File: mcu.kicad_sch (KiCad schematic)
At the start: 141 parts, among them Q10 BSS138W, Q3 BSS138W, Q4 BSS138W, Q5 BSS138W, Q6 BSS138W, Q7 BSS138W, Q8 BSS138W, Q9 BSS138W, SW1 TS110926043, SW2 TS110926043, U1 PIC32CK1025GC01100-I/4SB, X2 Q13FC13500004, X3 X322512MSB4SI

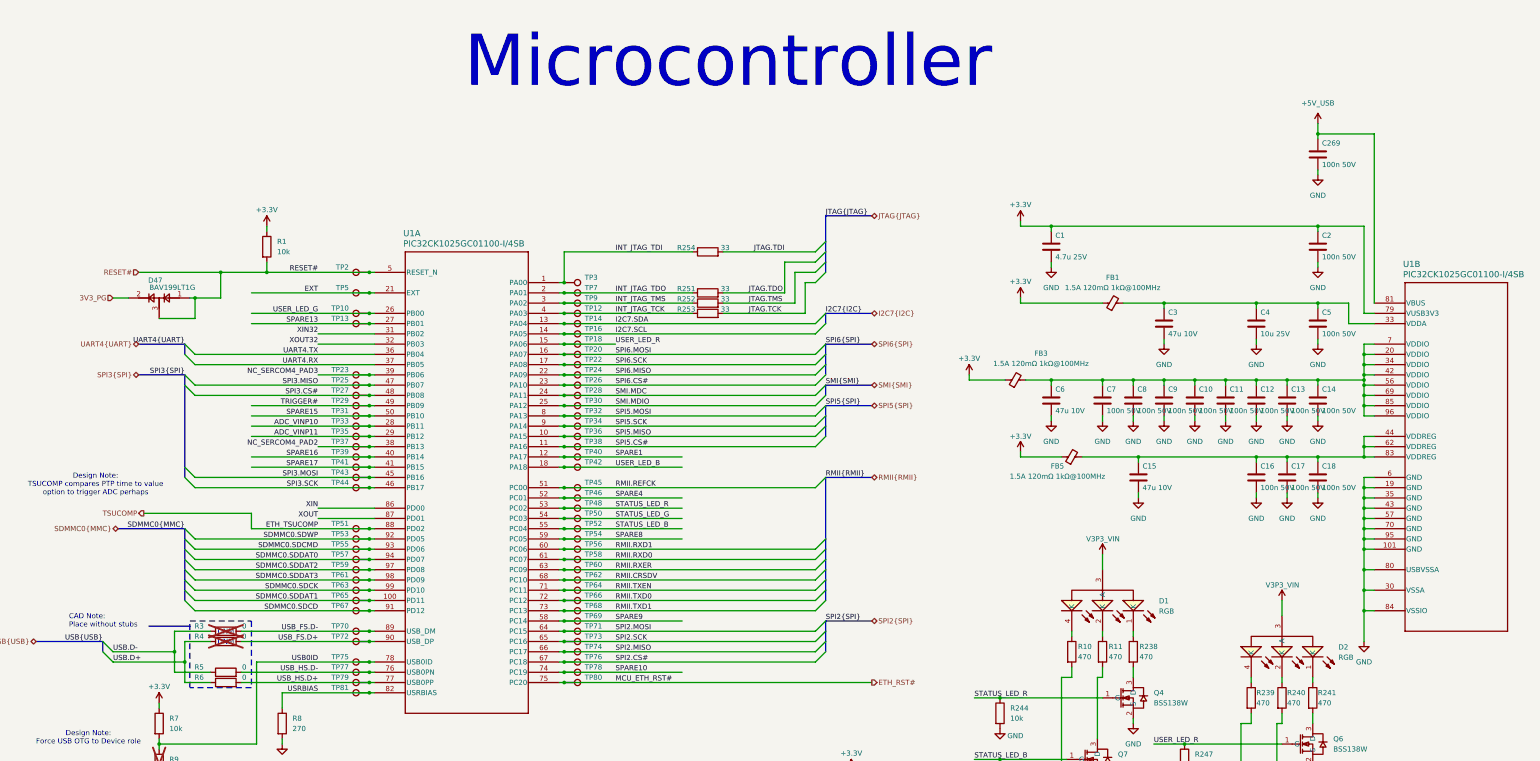
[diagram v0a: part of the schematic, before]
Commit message: fixed some more schematic review
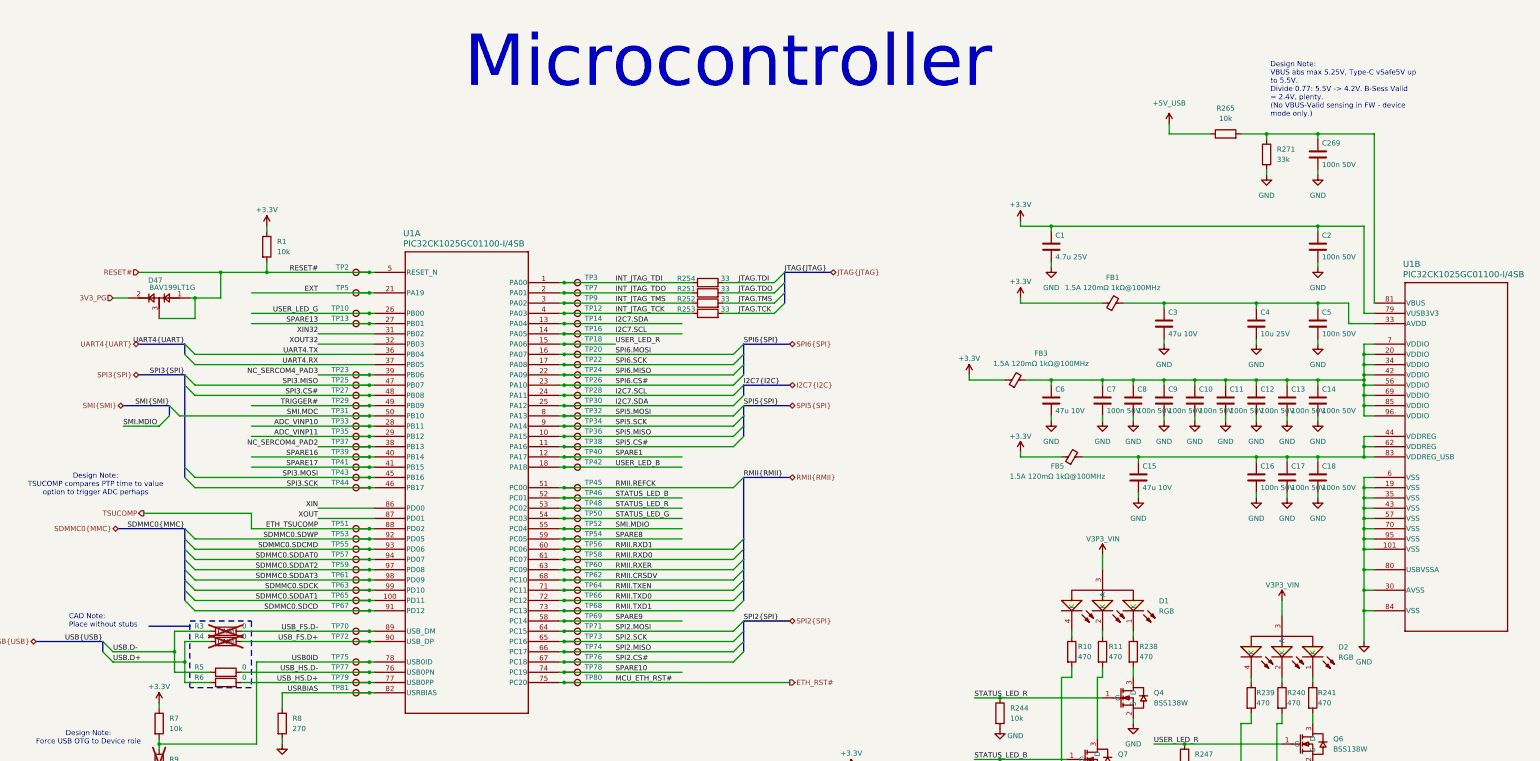
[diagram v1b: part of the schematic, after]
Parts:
- added R265: 10k, Resistor_SMD:R_0402_1005Metric, symbol Device:R
- added R271: 33k, Resistor_SMD:R_0603_1608Metric, symbol Device:R
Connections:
- net SPARE15 is gone; now on net SMI.MDC: TP31.1, U1.50 (PB10)
- net SPARE4 is gone; now on net STATUS_LED_B: TP46.1, U1.52 (PC01)
- net +5V_USB: now also R265.1; no longer C269.1, U1.81 (VBUS)
- net GND: now also R271.2
- net I2C7.SCL: now also TP28.1, U1.24 (PA11)
- net I2C7.SDA: now also TP30.1, U1.25 (PA12)
- net SMI.MDC: no longer TP28.1, U1.24 (PA11)
- net SMI.MDIO: now also TP52.1, U1.55 (PC04); no longer TP30.1, U1.25 (PA12)
- net STATUS_LED_B: no longer TP52.1, U1.55 (PC04)
- new net: C269.1, R265.2, R271.1, U1.81 (VBUS)
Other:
- moved on the sheet: R254

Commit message: did a bit of placement
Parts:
- removed TP45, TP54, TP56, TP58, TP62: TestPoint, TestPoint:TestPoint_THTPad_D1.0mm_Drill0.5mm, symbol Connector:TestPoint

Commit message: did some layout
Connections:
- net MCU_VDDREG: now reaches C15.1, C16.1, C17.1, C18.1, FB5.2, U1.44 (VDDREG), U1.62 (VDDREG), U1.83 (VDDREG_USB)
- net MCU_VDDIO: now reaches C10.1, C11.1, C12.1, C13.1, C14.1, C6.1, C7.1, C8.1, C9.1, FB3.2, U1.20 (VDDIO), U1.34 (VDDIO), U1.42 (VDDIO), U1.56 (VDDIO), U1.69 (VDDIO), U1.7 (VDDIO), U1.85 (VDDIO), U1.96 (VDDIO)
- net MCU_AVDD: now reaches C3.1, C4.1, C5.1, FB1.2, U1.33 (AVDD)
- net MCU_VBUS: now reaches C269.1, R265.2, R271.1, U1.81 (VBUS)
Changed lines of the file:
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@@
 		)
 	)
+	(label "MCU_VDDIO"
+		(at 318.77 116.84 0)
+		(effects
+			(font
+				(size 1.27 1.27)
+			)
+			(justify left bottom)
+		)
+	)
 	(label "SDMMC0.SDDAT0"
 		(at 100.33 161.29 180)
@@
 		)
 	)
+	(label "MCU_AVDD"
+		(at 320.04 97.79 0)
+		(effects
+			(font
+				(size 1.27 1.27)
+			)
+			(justify left bottom)
+		)
+	)
 	(label "RMII.RXER"
 		(at 173.99 163.83 0)
@@
 		)
 	)
+	(label "MCU_VBUS"
+		(at 341.63 55.88 0)
+		(effects
+			(font
+				(size 1.27 1.27)
+			)
+			(justify left bottom)
+		)
+	)
 	(label "TRIGGER#"
 		(at 229.87 224.79 180)
@@
 		)
 	)
+	(label "MCU_VDDREG"
+		(at 317.5 135.89 0)
+		(effects
+			(font
+				(size 1.27 1.27)
+			)
+			(justify left bottom)
+		)
+	)
 	(label "JTAG.TDO"
 		(at 204.47 95.25 0)
@@
 		)
 	)
+	(embedded_fonts no)
 )

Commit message: did a lot of layout
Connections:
- net I2C7.SCL: no longer TP16.1, U1.14 (PA05)
- net I2C7.SDA: no longer TP14.1, U1.13 (PA04)
- new net NC_PA4: TP14.1, U1.13 (PA04)
- new net NC_PA5: TP16.1, U1.14 (PA05)
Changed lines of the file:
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@@
 		)
 	)
-	(label "I2C7.SDA"
+	(label "NC_PA4"
 		(at 173.99 102.87 0)
 		(effects
 			(font
 				(size 1.27 1.27)
+				(color 0 18 255 1)
 			)
 			(justify left bottom)
@@
 		)
 	)
-	(label "I2C7.SCL"
+	(label "NC_PA5"
 		(at 173.99 105.41 0)
 		(effects
 			(font
 				(size 1.27 1.27)
-			)
-			(justify left bottom)
+				(color 6 0 255 1)
+			)
+			(justify left bottom)

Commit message: did some review cleanup
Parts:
- R271: footprint Resistor_SMD:R_0603_1608Metric -> Resistor_SMD:R_0402_1005Metric
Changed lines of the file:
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@@
 			)
 		)
-		(property "Footprint" "Resistor_SMD:R_0603_1608Metric"
+		(property "Footprint" "Resistor_SMD:R_0402_1005Metric"
 			(at 333.502 60.96 90)
 			(hide yes)
@@
 		)
 	)
-	(embedded_fonts no)
 )

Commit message: cleaned up the schematic review and cleared ERC
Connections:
- net TSUCOMP renamed ETH_TSUCOMP
